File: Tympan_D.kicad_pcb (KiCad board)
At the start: 4 copper layers, 38 x 74 mm, 108 parts, among them IC1 MK66FX1M0VMD18, IC2 MKL02Z32VFG4, IC3 BC127, J1 SJ-3523-SMT-TR, J2 SJ-3524-SMT-TR-PI, P1 USB_OTG, P2 CONN_01X06, P3 CONN_01X06, P4 CONN_01X06, P5 CONN_01X06, Q1 Q_PNP_BEC, SW1 CL-SB-22A, SW2 TACT_SWITCH, U1 LP5907MFX-3.3, U2 TLV320AIC3206IRSBT, U3 74LVC1G66, U4 LP5907MFX-1.8, Y1 32.768kHz, Y2 16MHz

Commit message: Updated with latest version of the hardware
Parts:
- removed ? (x2): MountingHole_2.2mm_M2, Mounting_Holes:MountingHole_2.2mm_M2
- removed C36: 1uF, Capacitors_SMD:C_0402
- removed C38: 4.7uF, Capacitors_SMD:C_0402
- removed Q1: Q_PNP_BEC, Tympan:SC-70-3
- removed R22: 2, Tympan:1020_(Reversed)
- removed R24: 0.22, Capacitors_SMD:C_0603
- added D1: APHB1608SGNC, Tympan:ABHB1608S, F.Cu at (121.3, 118.5)
- added G***: LOGO, Graphics:Tympan_LOGO, F.Cu at (128.4, 99.7)
- added G***: LOGO, Graphics:Tympan_LOGO, B.Cu at (134.0, 65.0)
- added G***: LOGO, Graphics:oshwa-logo-gear, B.Cu at (145.2, 99.8)
- added P10: CONN_01X01, Tympan:NPTH_2.4mm, F.Cu at (117.3, 54.5)
- added P6: CONN_01X03, Pin_Headers:Pin_Header_Straight_1x03_Pitch2.00mm, F.Cu at (120.7, 107.7)
- added P7: CONN_01X01, Tympan:NPTH_2.4mm, F.Cu at (146.6, 118.2)
- added P8: CONN_01X01, Tympan:NPTH_2.4mm, F.Cu at (117.6, 118.2)
- added P9: CONN_01X01, Tympan:NPTH_2.4mm, F.Cu at (150.3, 54.5)
- added R1: 1K, Resistors_SMD:R_0402, F.Cu at (118.6, 114.8)
- added R11: 1K, Resistors_SMD:R_0402, F.Cu at (119.6, 114.8)
- added R8: 2.2K, Resistors_SMD:R_0402, F.Cu at (119.0, 109.5)
- added U5: MCP73831, TO_SOT_Packages_SMD:SOT-23-5, F.Cu at (119.6, 112.0)
- BT1: value LiPo -> 4UCON-20519; footprint Solutions:Hirose_DF13A_2P_1.25H -> Solutions:4UCON-0217-20519
- C12, C13: value 0.1uF -> 2.2uF
- C14: value 1uF -> 0.1uF
- C17, C19: value 2.2uF -> 1uF
- L1, L2: value 600 -> 600R
- MIC1, MIC2: value SPH1642HT5H-1 -> SPM0687LR5H-1; footprint Tympan:SPH1642HT5H -> Tympan:SPM0687LR5H-1; moved to B.Cu
- R10, R2, R3, R4, R5, R6, R7, R9: value 33 -> 33R; footprint Resistors_SMD:R_0201_NoSilk -> Resistors_SMD:R_0402
- R12, R13: value 0 -> 0R
- R18, R21: value 220 -> 240R
- R25: value 470 -> 470R
- R34, R35, R36: value 240 -> 240R
- moved R12 5.10 mm to (133.7, 58.6)
- moved R13 5.10 mm to (133.7, 57.3)
- moved R14 5.10 mm to (133.7, 59.9)
- moved R17 5.10 mm to (133.7, 56.0)
- moved C16 4.35 mm to (149.8, 67.7)
- moved C19 3.46 mm to (117.8, 66.7)
- moved C18 3.07 mm to (117.8, 67.7), turned to 0 degrees
- moved D5 2.91 mm to (139.8, 112.1), turned to 270 degrees
- moved C17 2.90 mm to (149.8, 66.7)
- moved P5 2.72 mm to (116.6, 71.8)
- moved P4 2.52 mm to (119.2, 71.8)
- moved BT1 2.00 mm to (133.7, 113.9), turned to 90 degrees
- moved C13 1.54 mm to (132.6, 67.0)
- moved C12 1.45 mm to (133.4, 67.0)
- moved MIC2 1.28 mm to (117.8, 65.0), turned to 0 degrees
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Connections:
- net /IN3_L renamed Net-(C12-Pad1)
- net /IN3_R renamed Net-(C13-Pad1)
- C15 pad 1: /V_USB -> /USB
- C16 pad 2: +1V8 -> +3V3
- C18 pad 2: +1V8 -> +3V3
- C3 pad 2: +BATT -> +3V3
- C35 pad 1: Net-(C35-Pad1) -> /V_USB
- C40 pad 1: Net-(C35-Pad1) -> /V_USB
- C41 pad 1: Net-(C35-Pad1) -> /V_USB
- D4 pad 2: Net-(C35-Pad1) -> /V_USB
- IC1 pad B12: /POT -> /DIN_1
- IC1 pad B7: /SDA_1 -> /DOUT_1
- IC1 pad C12: Net-(IC1-PadC12) -> GND
- IC1 pad C7: /SCL_1 -> Net-(IC1-PadC7)
- IC1 pad H11: Net-(IC1-PadH11) -> /M_BIAS_1
- IC1 pad J11: Net-(IC1-PadJ11) -> /nRESET_1
- IC1 pad J9: Net-(IC1-PadJ9) -> /SDA2
- IC1 pad K11: Net-(IC1-PadK11) -> /POT
- IC1 pad K9: Net-(IC1-PadK9) -> /SCL2
- IC1 pad M1: Net-(IC1-PadM1) -> /BT_PIO0
- IC1 pad M4: /BT_PIO4 -> /BT_PIO5
- IC3 pad 23: Net-(IC3-Pad23) -> /BT_PIO0
- IC3 pad 25: Net-(IC3-Pad25) -> /BT_PIO5
- IC3 pad 26: /BT_PIO4 -> Net-(IC3-Pad26)
- IC3 pad 30: Net-(C36-Pad1) -> +3V3
- IC3 pad 31: +BATT -> +3V3
- IC3 pad 32: +BATT -> +3V3
- IC3 pad 33: VPP -> +3V3
- L3 pad 1: /V_USB -> /USB
- L3 pad 2: Net-(C35-Pad1) -> /V_USB
- MIC1 pad 1: GND -> Net-(C17-Pad2)
- MIC1 pad 4: Net-(C17-Pad2) -> +3V3
- MIC1 pad 5: GND -> Net-(MIC1-Pad5)
- MIC2 pad 1: GND -> Net-(C19-Pad2)
- MIC2 pad 4: Net-(C19-Pad2) -> +3V3
- MIC2 pad 5: GND -> Net-(MIC2-Pad5)
- P1 pad 1: /V_USB -> /USB
- P3 pad 2: /DOUT -> /DOUT_1
- P3 pad 3: /DIN -> /DIN_1
- P3 pad 4: /SDA_1 -> /SDA2
- P3 pad 5: /SCL_1 -> /SCL2
- P4 pad 1: +1V8 -> /M_BIAS_1
- P4 pad 5: /nRESET -> /nRESET_1
- SW2 pad 4: GND -> Net-(SW2-Pad4)
- U2 pad 30: +BATT -> +3V3
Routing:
- net +BATT: track 66.6 -> 20.5 mm, vias 4 -> 1
- net /DIN_1: track 0.00 -> 35.3 mm, vias 0 -> 1
- net /M_BIAS_1: track 0.00 -> 33.4 mm, vias 0 -> 2
- net /SCL2: track 0.00 -> 31.2 mm, vias 0 -> 5
- net /SDA2: track 0.00 -> 31.2 mm, vias 0 -> 3
- net /DOUT_1: track 0.00 -> 29.7 mm, vias 0 -> 3
- net /SDA_1: track 25.1 -> 0.00 mm, vias 3 -> 0
- net /nRESET_1: track 0.00 -> 24.0 mm, vias 0 -> 2
- net /SCL_1: track 23.3 -> 0.00 mm, vias 3 -> 0
- net /DIN: track 32.9 -> 12.2 mm, vias 4 -> 3
- net /nRESET: track 24.7 -> 6.62 mm
- net /DOUT: track 34.7 -> 16.8 mm, vias 4 -> 3
- net /BT_PIO4: track 13.0 -> 0.00 mm, vias 1 -> 0
- net +1V8: track 28.8 -> 16.2 mm, vias 9 -> 6
- net +3V3: track 32.2 -> 44.6 mm, vias 8 -> 12
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- removed copper zone on B.Cu, net +BATT
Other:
- outline, holes or cut-outs redrawn
- board text added: "1V8/M_BIAS_1 IN1_R/MCLK IN1_L/BCLK LOL/WCLK LOR/RST_1 GND/GND"
- board text added: "BLUETOOTH STATUS"
- board text added: "CHARGE"
- board text added: "Cut trace btw VPP/V_BAT to attach your own RTC battery to V_BAT and GND"
- board text added: "Designed in Brooklyn, NY"
- board text added: "GND VPP V_BAT"
- board text added: "L"
- board text added: "OUTPUT"
- board text added: "TX_3/3V3 RX_3/DOUT MISO_2/DIN MOSI_2/SDA_1 SCK_2/SCL_1 SS_2/GND"
- board text added: "TYMPAN RevD"
- board text added: "V"
- board text added: "legit thing"
- board text added: "o"
- board text added: "www.tympan.org github.com/tympan"
- board text removed: "500mAh Battery"
- board text removed: "PHONES"

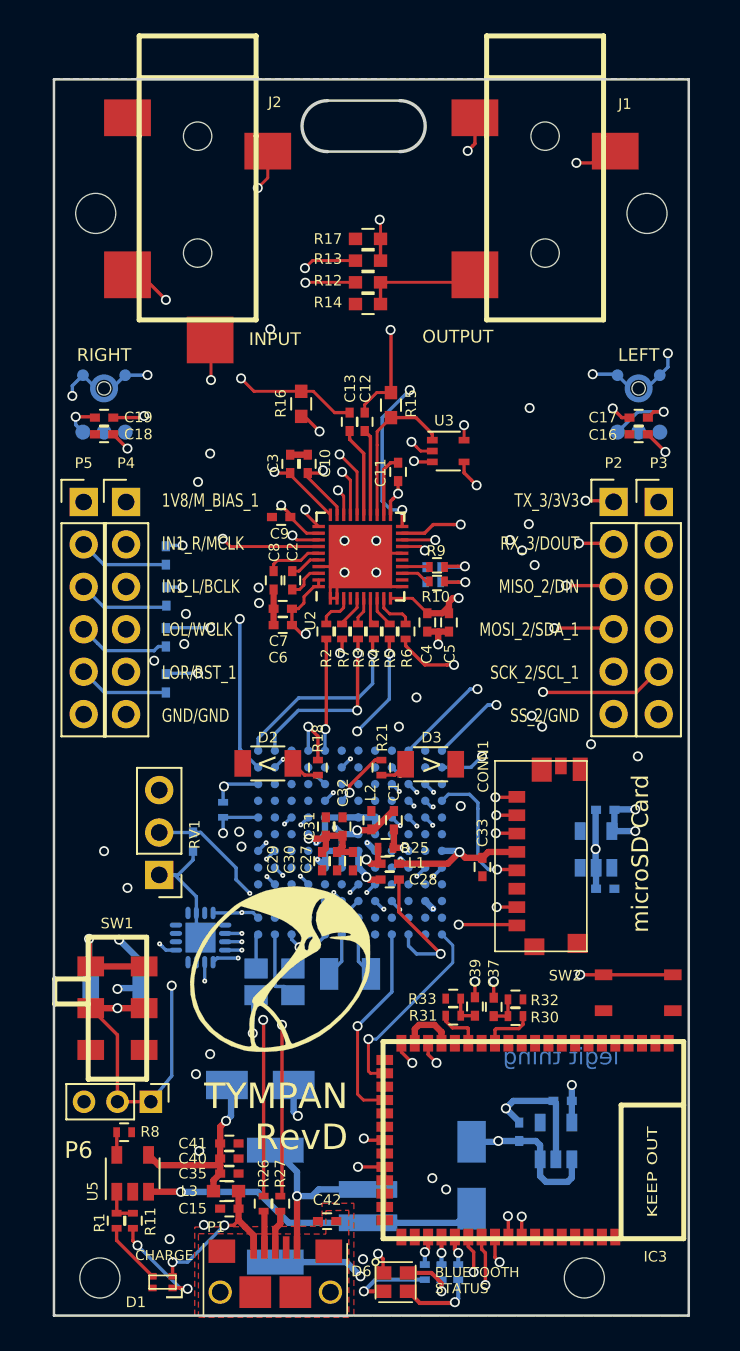
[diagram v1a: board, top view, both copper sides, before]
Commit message: Adjusted tracks. Switched PIO0
Moved PIO0 to a digital pin
Moved tracks from under the xtal per PJRC
Cleaned up speaker out ground trace
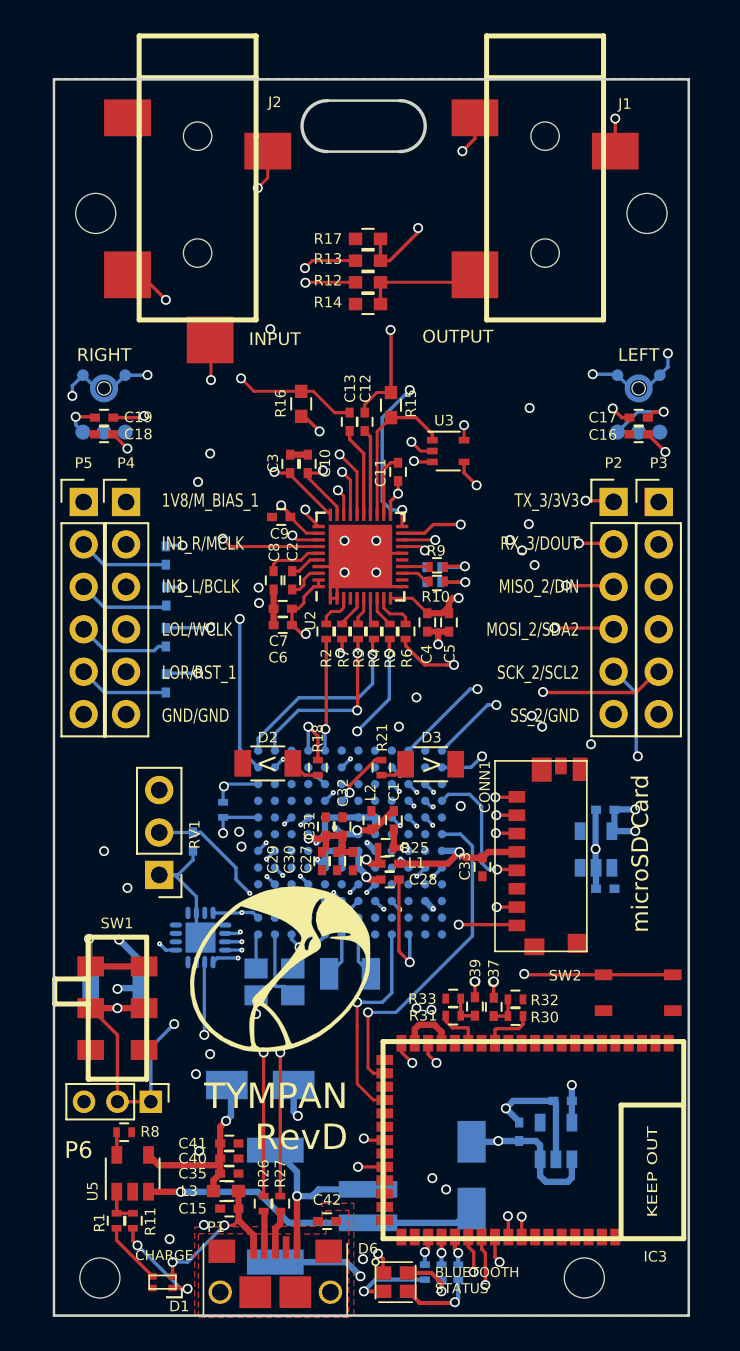
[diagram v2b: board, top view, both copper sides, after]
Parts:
- R26, R27: value 33 -> 33R
- moved G*** 1.41 mm to (146.0, 100.9)
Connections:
- IC1 pad F1: Net-(IC1-PadF1) -> /BT_PIO0
- IC1 pad M1: /BT_PIO0 -> Net-(IC1-PadM1)
- SW2 pad 4: Net-(SW2-Pad4) -> GND
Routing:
- net /BT_PIO0: track 11.9 -> 20.1 mm
- net /PROG: track 29.6 -> 34.3 mm
- net GND: track 120.6 -> 122.9 mm
- net /PTA0: track 12.4 -> 10.6 mm
- net /PTA2: track 11.9 -> 10.3 mm
- net Net-(C28-Pad2): track 8.30 -> 6.92 mm
- net Net-(C12-Pad2): track 24.5 -> 23.4 mm
- net Net-(C13-Pad2): track 23.0 -> 22.0 mm
- net /USB0_D+: track 28.4 -> 27.5 mm
- net /USB0_D-: track 28.5 -> 27.7 mm
- net /BT_PIO5: track 12.2 -> 12.7 mm
- net /BCLK: track 27.1 -> 26.9 mm, vias 3 -> 2
- net /MCLK: track 25.6 -> 25.8 mm, vias 4 -> 3
- net /WCLK: track 28.0 -> 27.9 mm, vias 2 -> 1
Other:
- board text added: "3V3 A20 GND"
- board text added: "Cut trace btw VPP | V_BAT to attach your own RTC battery to V_BAT | GND"
- board text added: "TX_3/3V3 RX_3/DOUT MISO_2/DIN MOSI_2/SDA2 SCK_2/SCL2 SS_2/GND"
- board text removed: "3V3 A1 GND"
- board text removed: "Cut trace btw VPP/V_BAT to attach your own RTC battery to V_BAT and GND"
- board text removed: "TX_3/3V3 RX_3/DOUT MISO_2/DIN MOSI_2/SDA_1 SCK_2/SCL_1 SS_2/GND"
- board text removed: "legit thing"

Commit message: Updated changes from client
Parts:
- added J3: alt Power Pads, Tympan:alt Power Pads, B.Cu at (141.9, 103.7)
- P10, P8, P9: footprint Tympan:NPTH_2.4mm -> Tympan:NPTH_3.2mm
- moved G*** 27.1 mm to (131.1, 78.2)
- moved C20 3.07 mm to (146.7, 92.1)
- moved C22 3.07 mm to (146.7, 87.4)
- moved U4 3.07 mm to (146.2, 89.7)
- moved G*** 2.00 mm to (134.0, 63.0)
- moved RV1 1.00 mm to (120.2, 94.1)
- moved P10 0.37 mm to (117.6, 54.2)
- moved P9 0.37 mm to (150.6, 54.2)
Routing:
- net +BATT: track 20.5 -> 35.1 mm, vias 1 -> 3
- net GND: track 122.9 -> 129.1 mm, vias 24 -> 26
- net +3V3: track 44.6 -> 46.8 mm, vias 12 -> 14
- net /M_BIAS_1: track 33.4 -> 35.3 mm
- net /nRESET_1: track 24.0 -> 25.4 mm
- net /POT: track 9.15 -> 10.2 mm
- net /SCK_2: track 17.7 -> 17.1 mm
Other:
- outline, holes or cut-outs redrawn
- board text added: "Alt Power 12V Max"
- board text added: "GND BATT"
- board text added: "McMaster 95844A275"

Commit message: Update to readme
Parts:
- added V_USB: DNP, Capacitors_SMD:C_0603, F.Cu at (122.9, 111.5)
- U1: value LP5907MFX-3.3 -> AP2210K-3.3TRG1
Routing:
- net /VREGEN: track 34.2 -> 33.4 mm
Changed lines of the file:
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@@
     (thickness 1.6)
     (drawings 76)
-    (tracks 1326)
+    (tracks 1327)
     (zones 0)
-    (modules 115)
+    (modules 116)
     (nets 228)
   )
@@
     (mod_text_size 0.635 0.635)
     (mod_text_width 0.127)
-    (pad_size 3 3)
-    (pad_drill 3)
+    (pad_size 1.5 3.4)
+    (pad_drill 0)
     (pad_to_mask_clearance 0.2)
     (solder_mask_min_width 0.25)
@@
     (tags "resistor 0402")
     (attr smd)
-    (fp_text reference R26 (at 1.8 0 90) (layer F.SilkS)
+    (fp_text reference R26 (at 0.35 2.1 90) (layer F.SilkS)
       (effects (font (size 0.635 0.635) (thickness 0.127)))
     )
@@
     (tags "resistor 0402")
     (attr smd)
-    (fp_text reference R27 (at 1.8 0 90) (layer F.SilkS)
+    (fp_text reference R27 (at 0.35 2.15 90) (layer F.SilkS)
       (effects (font (size 0.635 0.635) (thickness 0.127)))
     )
@@
       (effects (font (size 0.635 0.635) (thickness 0.127)) (justify mirror))
     )
-    (fp_text value LP5907MFX-3.3 (at 0 -2.9 90) (layer B.Fab)
+    (fp_text value AP2210K-3.3TRG1 (at 0 -2.9 90) (layer B.Fab)
       (effects (font (size 1 1) (thickness 0.15)) (justify mirror))
     )
@@
     (tags "capacitor 0402")
     (attr smd)
-    (fp_text reference C35 (at -2.2 0) (layer F.SilkS)
+    (fp_text reference C35 (at 2 0) (layer F.SilkS)
       (effects (font (size 0.635 0.635) (thickness 0.127)))
     )
@@
     (tags "capacitor 0402")
     (attr smd)
-    (fp_text reference C40 (at -2.2 0) (layer F.SilkS)
+    (fp_text reference C40 (at 1.95 -0.05) (layer F.SilkS)
       (effects (font (size 0.635 0.635) (thickness 0.127)))
     )
@@
     (tags "capacitor 0402")
     (attr smd)
-    (fp_text reference C41 (at -2.2 0) (layer F.SilkS)
+    (fp_text reference C41 (at 1.95 0.05) (layer F.SilkS)
       (effects (font (size 0.635 0.635) (thickness 0.127)))
     )
@@
     (tags "capacitor 0402")
     (attr smd)
-    (fp_text reference C42 (at 0 -1.27) (layer F.SilkS)
+    (fp_text reference C42 (at -2 0) (layer F.SilkS)
       (effects (font (size 0.635 0.635) (thickness 0.127)))
     )
@@
       (net 1 GND))
   )
+  (module Capacitors_SMD:C_0603 (layer F.Cu)
+    (at 122.9 111.48)
+    (descr "Capacitor SMD 0603, reflow soldering, AVX (see smccp.pdf)")
+    (tags "capacitor 0603")
+    (attr smd)
+    (fp_text reference V_USB (at 0 -1.5) (layer F.SilkS)
+      (effects (font (size 0.635 0.635) (thickness 0.127)))
+    )
+    (fp_text value DNP (at 0 1.5) (layer F.Fab)
+      (effects (font (size 1 1) (thickness 0.15)))
+    )
+    (fp_text user %R (at 0 0) (layer F.Fab)
+      (effects (font (size 0.3 0.3) (thickness 0.075)))
+    )
+    (fp_line (start -0.8 0.4) (end -0.8 -0.4) (layer F.Fab) (width 0.1))
+    (fp_line (start 0.8 0.4) (end -0.8 0.4) (layer F.Fab) (width 0.1))
+    (fp_line (start 0.8 -0.4) (end 0.8 0.4) (layer F.Fab) (width 0.1))
+    (fp_line (start -0.8 -0.4) (end 0.8 -0.4) (layer F.Fab) (width 0.1))
+    (fp_line (start -0.35 -0.6) (end 0.35 -0.6) (layer F.SilkS) (width 0.12))
+    (fp_line (start 0.35 0.6) (end -0.35 0.6) (layer F.SilkS) (width 0.12))
+    (fp_line (start -1.4 -0.65) (end 1.4 -0.65) (layer F.CrtYd) (width 0.05))
+    (fp_line (start -1.4 -0.65) (end -1.4 0.65) (layer F.CrtYd) (width 0.05))
+    (fp_line (start 1.4 0.65) (end 1.4 -0.65) (layer F.CrtYd) (width 0.05))
+    (fp_line (start 1.4 0.65) (end -1.4 0.65) (layer F.CrtYd) (width 0.05))
+    (pad 1 smd rect (at -0.75 0) (size 0.8 0.75) (layers F.Cu F.Paste F.Mask)
+      (net 179 /V_USB))
+    (pad 2 smd rect (at 0.75 0) (size 0.8 0.75) (layers F.Cu F.Paste F.Mask)
+      (net 179 /V_USB))
+    (model Capacitors_SMD.3dshapes/C_0603.wrl
+      (at (xyz 0 0 0))
+      (scale (xyz 1 1 1))
+      (rotate (xyz 0 0 0))
+    )
+  )
   (gr_text "McMaster 95844A275" (at 158.65 54.53 90) (layer Dwgs.User)
     (effects (font (size 1 1) (thickness 0.2)))
@@
   (segment (start 133.5 109.98) (end 133.4 109.88) (width 0.2032) (layer F.Cu) (net 187))
   (via (at 133.4 109.88) (size 0.6) (drill 0.4) (layers F.Cu B.Cu) (net 187))
-  (segment (start 133.4 109.88) (end 132.65 110.63) (width 0.2032) (layer In2.Cu) (net 187))
-  (segment (start 132.65 110.63) (end 123.55 110.63) (width 0.2032) (layer In2.Cu) (net 187))
-  (via (at 123.55 110.63) (size 0.6) (drill 0.4) (layers F.Cu B.Cu) (net 187))
-  (segment (start 123.55 110.63) (end 123.55 107.53) (width 0.2032) (layer In1.Cu) (net 187))
-  (segment (start 123.55 107.53) (end 124.975 106.105) (width 0.2032) (layer In1.Cu) (net 187))
-  (segment (start 124.975 106.105) (end 124.975 91.605) (width 0.2032) (layer In1.Cu) (net 187))
   (segment (start 124.975 91.605) (end 124.975 90.655) (width 0.2032) (layer B.Cu) (net 187))
   (via (at 124.975 91.605) (size 0.6) (drill 0.4) (layers F.Cu B.Cu) (net 187))
@@
   (segment (start 127.06444 90.655) (end 127.0749 90.66546) (width 0.2032) (layer B.Cu) (net 187))
   (segment (start 134.65 109.98) (end 134.6 109.93) (width 0.25) (layer F.Cu) (net 187))
+  (segment (start 123.55 109.655736) (end 123.55 110.08) (width 0.2032) (layer In1.Cu) (net 187))
+  (segment (start 124.975 91.605) (end 124.975 106.105) (width 0.2032) (layer In1.Cu) (net 187))
+  (segment (start 123.75 109.88) (end 123.55 110.08) (width 0.2032) (layer In2.Cu) (net 187))
+  (segment (start 124.975 106.105) (end 123.55 107.53) (width 0.2032) (layer In1.Cu) (net 187))
+  (segment (start 123.55 107.53) (end 123.55 109.655736) (width 0.2032) (layer In1.Cu) (net 187))
+  (segment (start 133.4 109.88) (end 123.75 109.88) (width 0.2032) (layer In2.Cu) (net 187))
+  (via (at 123.55 110.08) (size 0.6) (drill 0.4) (layers F.Cu B.Cu) (net 187))
   (segment (start 137.25 115.78) (end 137.25 116.48) (width 0.25) (layer F.Cu) (net 188))
   (segment (start 137.05 116.68) (end 137.05 117.43) (width 0.25) (layer B.Cu) (net 188))

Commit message: Final changes to PCB
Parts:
- moved D1 2.06 mm to (122.5, 116.8), turned to 270 degrees
- moved SW1 1.13 mm to (117.5, 102.1)
- moved C5 0.35 mm to (138.8, 79.0)
- moved V_USB 0.05 mm to (122.8, 111.5)
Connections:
- P2 pad 1: /TX_3 -> /PDM_DAT
- P2 pad 2: /RX_3 -> /PDM_CLK
- U2 pad 12: Net-(U2-Pad12) -> /PDM_CLK
- U2 pad 15: Net-(U2-Pad15) -> /PDM_DAT
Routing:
- net /TX_3: track 29.3 -> 0.00 mm, vias 3 -> 0
- net /RX_3: track 27.7 -> 0.00 mm, vias 3 -> 0
- net /PDM_CLK: track 0.00 -> 15.8 mm, vias 0 -> 2
- net /PDM_DAT: track 0.00 -> 14.1 mm, vias 0 -> 1
- net /BT_TX: track 53.9 -> 51.7 mm
- net Net-(D1-Pad1): track 6.14 -> 3.93 mm, vias 2 -> 0
- net /SCL/SS: track 31.6 -> 29.8 mm
- net /SDA/MOSI: track 33.2 -> 31.5 mm
- net GND: track 129.1 -> 130.4 mm, vias 26 -> 27
- net /IN1_R: track 51.4 -> 52.7 mm
- net /IN1_L: track 51.2 -> 52.1 mm
- net Net-(D1-Pad4): track 3.77 -> 4.43 mm
- net +3V3: track 46.8 -> 46.2 mm
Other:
- board text added: "OD 3mm"
